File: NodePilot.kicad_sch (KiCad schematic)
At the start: 33 parts, among them K1 SRD-05VDC-SL-C, Q1 2N3904, Q2 2N3904, Q3 2N3904, Q4 2N3904, T1 1:1 600R, T2 1:1 600R, U1 PC817, U2 PC817

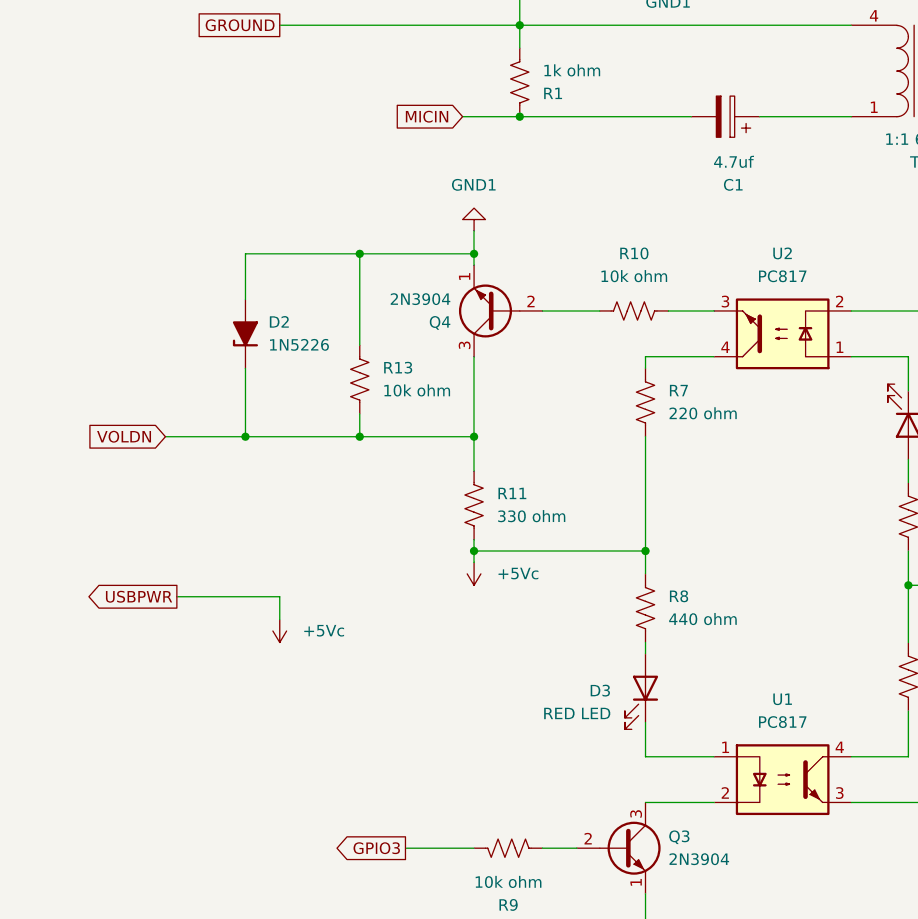
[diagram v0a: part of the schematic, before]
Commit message: usb instead of usbinvert
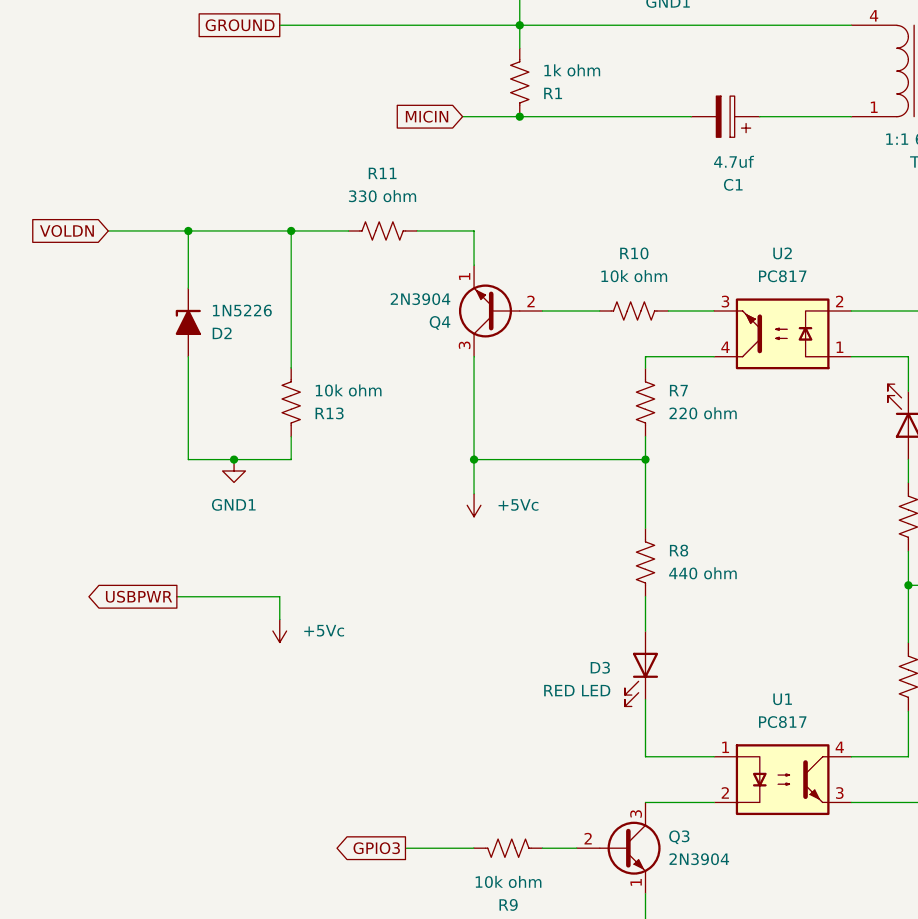
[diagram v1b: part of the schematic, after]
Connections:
- net +5Vc: now also Q4.3 (C); no longer R11.2
- net GND1: no longer Q4.1 (E)
- net VOLDN: no longer Q4.3 (C)
- new net: Q4.1 (E), R11.2
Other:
- moved on the sheet: D2, D3, R13, R8

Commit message: name fix
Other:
- title: NodePilot By Radiosanda -> NodePilot By S21TIP
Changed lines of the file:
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@@
 	(paper "A4")
 	(title_block
-		(title "NodePilot By Radiosanda")
+		(title "NodePilot By S21TIP")
 		(date "2025-11-30")
 		(rev "2.1")

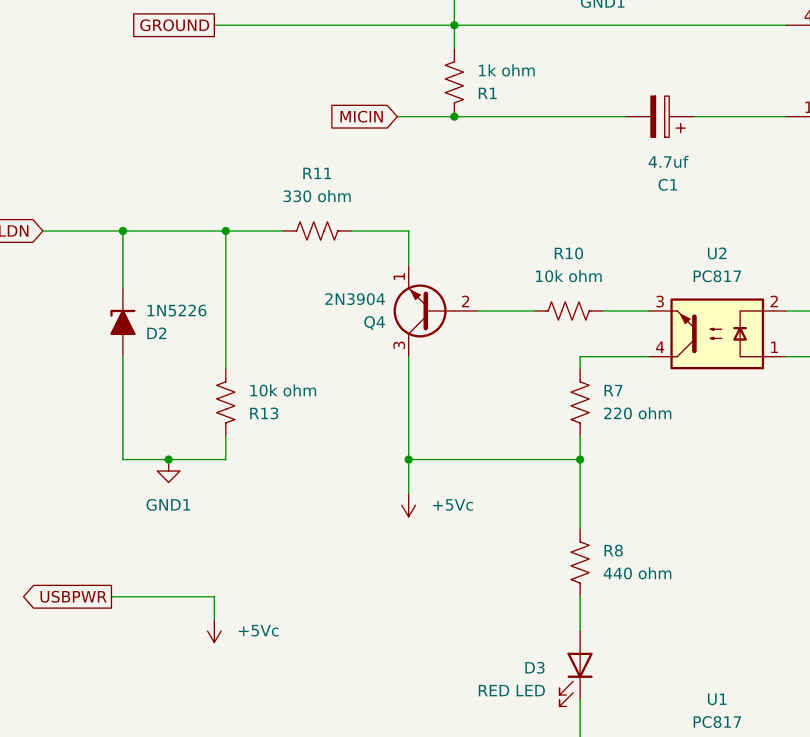
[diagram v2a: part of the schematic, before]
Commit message: 3904 load config fix
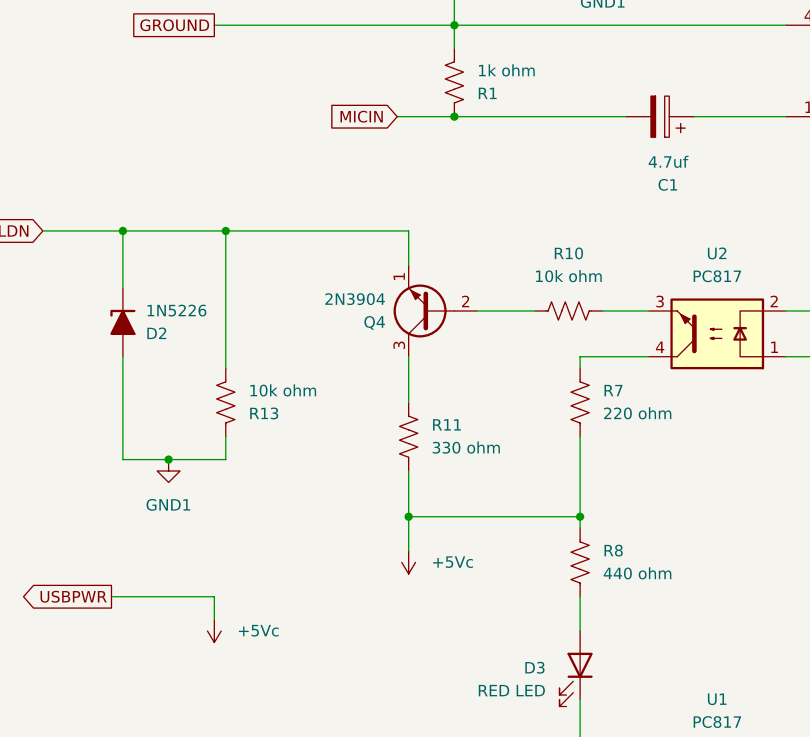
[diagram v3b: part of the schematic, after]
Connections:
- net +5Vc: now also R11.2; no longer Q4.3 (C)
- net VOLDN: now also Q4.1 (E); no longer R11.1
- new net: Q4.3 (C), R11.1
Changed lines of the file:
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@@
-	)
-	(junction
-		(at 72.39 105.41)
-		(diameter 0)
-		(color 0 0 0 0)
 	)
 	(junction
@@
 	)
 	(junction
+		(at 72.39 111.76)
+		(diameter 0)
+		(color 0 0 0 0)
+	)
+	(junction
 		(at 93.98 46.99)
 		(diameter 0)
@@
 	)
 	(junction
-		(at 91.44 105.41)
-		(diameter 0)
-		(color 0 0 0 0)
-	)
-	(junction
 		(at 134.62 119.38)
 		(diameter 0)
@@
 	)
 	(junction
+		(at 91.44 111.76)
+		(diameter 0)
+		(color 0 0 0 0)
+	)
+	(junction
 		(at 77.47 67.31)
 		(diameter 0)
@@
 	(wire
 		(pts
-			(xy 91.44 102.87) (xy 91.44 105.41)
-		)
-		(stroke
-			(width 0)
-			(type default)
-		)
-	)
-	(wire
-		(pts
 			(xy 156.21 93.98) (xy 151.13 93.98)
 		)
@@
 	(wire
 		(pts
+			(xy 91.44 111.76) (xy 91.44 113.03)
+		)
+		(stroke
+			(width 0)
+			(type default)
+		)
+	)
+	(wire
+		(pts
 			(xy 77.47 57.15) (xy 114.3 57.15)
 		)
@@
 	(wire
 		(pts
-			(xy 72.39 105.41) (xy 91.44 105.41)
+			(xy 72.39 111.76) (xy 91.44 111.76)
 		)
 		(stroke
@@
 	(wire
 		(pts
+			(xy 72.39 93.98) (xy 72.39 99.06)
+		)
+		(stroke
+			(width 0)
+			(type default)
+		)
+	)
+	(wire
+		(pts
 			(xy 72.39 80.01) (xy 72.39 83.82)
 		)
@@
 	(wire
 		(pts
+			(xy 72.39 111.76) (xy 72.39 115.57)
+		)
+		(stroke
+			(width 0)
+			(type default)
+		)
+	)
+	(wire
+		(pts
 			(xy 170.18 119.38) (xy 134.62 119.38)
 		)
@@
 	(wire
 		(pts
-			(xy 66.04 80.01) (xy 72.39 80.01)
-		)
-		(stroke
-			(width 0)
-			(type default)
-		)
-	)
-	(wire
-		(pts
 			(xy 71.12 67.31) (xy 77.47 67.31)
 		)
@@
 	(wire
 		(pts
-			(xy 72.39 93.98) (xy 72.39 105.41)
-		)
-		(stroke
-			(width 0)
-			(type default)
-		)
-	)
-	(wire
-		(pts
 			(xy 120.65 105.41) (xy 120.65 107.95)
 		)
@@
 	(wire
 		(pts
-			(xy 52.07 80.01) (xy 58.42 80.01)
+			(xy 52.07 80.01) (xy 72.39 80.01)
 		)
 		(stroke
@@
 	(wire
 		(pts
-			(xy 91.44 105.41) (xy 91.44 113.03)
-		)
-		(stroke
-			(width 0)
-			(type default)
-		)
-	)
-	(wire
-		(pts
 			(xy 170.18 135.89) (xy 170.18 138.43)
 		)
@@
 	(wire
 		(pts
+			(xy 91.44 102.87) (xy 91.44 111.76)
+		)
+		(stroke
+			(width 0)
+			(type default)
+		)
+	)
+	(wire
+		(pts
 			(xy 40.64 80.01) (xy 40.64 86.36)
 		)
@@
 	(wire
 		(pts
+			(xy 72.39 106.68) (xy 72.39 111.76)
+		)
+		(stroke
+			(width 0)
+			(type default)
+		)
+	)
+	(wire
+		(pts
 			(xy 180.34 135.89) (xy 180.34 139.7)
 		)
@@
 		(pts
 			(xy 144.78 67.31) (xy 157.48 67.31)
-		)
-		(stroke
-			(width 0)
-			(type default)
-		)
-	)
-	(wire
-		(pts
-			(xy 72.39 105.41) (xy 72.39 109.22)
 		)
 		(stroke
@@
 	(symbol
 		(lib_id "power:+5V")
-		(at 72.39 109.22 180)
+		(at 72.39 115.57 180)
 		(unit 1)
 		(exclude_from_sim no)
@@
 		(fields_autoplaced yes)
 		(property "Reference" "#PWR0101"
-			(at 72.39 105.41 0)
+			(at 72.39 111.76 0)
 			(effects
 				(font
@@
 		)
 		(property "Value" "+5Vc"
-			(at 74.93 110.4899 0)
+			(at 74.93 116.8399 0)
 			(effects
 				(font
@@
 		)
 		(property "Footprint" ""
-			(at 72.39 109.22 0)
+			(at 72.39 115.57 0)
 			(effects
 				(font
@@
 		)
 		(property "Datasheet" ""
-			(at 72.39 109.22 0)
+			(at 72.39 115.57 0)
 			(effects
 				(font
@@
 		)
 		(property "Description" "Power symbol creates a global label with name \"+5V\""
-			(at 72.39 109.22 0)
+			(at 72.39 115.57 0)
 			(effects
 				(font
@@
 	)
 	(symbol
-		(lib_id "Device:R_US")
-		(at 62.23 80.01 90)
-		(unit 1)
-		(exclude_from_sim no)
-		(in_bom yes)
-		(on_board yes)
-		(dnp no)
-		(fields_autoplaced yes)
-		(property "Reference" "R11"
-			(at 62.23 73.66 90)
-			(effects
-				(font
-					(size 1.27 1.27)
-				)
-			)
-		)
-		(property "Value" "330 ohm"
-			(at 62.23 76.2 90)
-			(effects
-				(font
-					(size 1.27 1.27)
-				)
-			)
-		)
-		(property "Footprint" ""
-			(at 62.484 78.994 90)
-			(effects
-				(font
-					(size 1.27 1.27)
-				)
-				(hide yes)
-			)
-		)
-		(property "Datasheet" "~"
-			(at 62.23 80.01 0)
-			(effects
-				(font
-					(size 1.27 1.27)
-				)
-				(hide yes)
-			)
-		)
-		(property "Description" "Resistor, US symbol"
-			(at 62.23 80.01 0)
-			(effects
-				(font
-					(size 1.27 1.27)
-				)
-				(hide yes)
-			)
-		)
-		(pin "1"
-		)
-		(pin "2"
-		)
-		(instances
-			(project ""
-				(path "/feb6dcc4-ba57-4640-ad64-1efd302ce012"
-					(reference "R11")
-					(unit 1)
-				)
-			)
-		)
-	)
-	(symbol
 		(lib_id "power:+5V")
 		(at 204.47 148.59 180)
@@
 					(unit 1)
 				)
+			)
+		)
+	)
+	(symbol
+		(lib_id "Device:R_US")
+		(at 72.39 102.87 0)
+		(unit 1)
+		(exclude_from_sim no)
+		(in_bom yes)
+		(on_board yes)
+		(dnp no)
+		(fields_autoplaced yes)
+		(property "Reference" "R11"
+			(at 74.93 101.5999 0)
+			(effects
+				(font
+					(size 1.27 1.27)
+				)
+				(justify left)
+			)
+		)
+		(property "Value" "330 ohm"
+			(at 74.93 104.1399 0)
+			(effects
+				(font
+					(size 1.27 1.27)
+				)
+				(justify left)
+			)
+		)
+		(property "Footprint" ""
+			(at 73.406 103.124 90)
+			(effects
+				(font
+					(size 1.27 1.27)
+				)
+				(hide yes)
+			)
+		)
+		(property "Datasheet" "~"
+			(at 72.39 102.87 0)
+			(effects
+				(font
+					(size 1.27 1.27)
+				)
+				(hide yes)
+			)
+		)
+		(property "Description" "Resistor, US symbol"
+			(at 72.39 102.87 0)
+			(effects
+				(font
+					(size 1.27 1.27)
+				)
+				(hide yes)
+			)
+		)
+		(pin "1"
+		)
+		(pin "2"
+		)
+		(instances
+			(project ""
+				(path "/feb6dcc4-ba57-4640-ad64-1efd302ce012"
+					(reference "R11")
+					(unit 1)
+				)

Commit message: version 3.0
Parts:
- removed Q2: 2N3904, Package_TO_SOT_THT:TO-92_Inline, symbol Transistor_BJT:2N3904
- removed R5: 10k ohm, symbol Device:R_US
- removed R6: 220 ohm, symbol Device:R_US
- removed R8: 440 ohm, symbol Device:R_US
- removed U1: PC817, Package_DIP:DIP-4_W7.62mm, symbol Isolator:PC817
- R2: value 440 ohm -> 330 ohm
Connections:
- net +5Vc: now also K1.5
- net +5Vr: no longer K1.5, R4.1
- net at R4.2: now also K1.2
- net at D3.1 (K): now also Q3.3 (C)
- net at D3.2 (A): now also R4.1
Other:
- moved on the sheet: K1, Q3, R9

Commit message: ver 3.1
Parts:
- removed R7: 220 ohm, symbol Device:R_US
- R13: value 10k ohm -> 22k ohm
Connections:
- net at U2.4: now also Q4.3 (C), R11.1
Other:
- moved on the sheet: R11
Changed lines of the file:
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@@
 	(title_block
 		(title "NodePilot By S21TIP")
-		(date "2025-12-11")
-		(rev "3.0")
+		(date "2025-12-12")
+		(rev "3.1")
+	)
+	(junction
+		(at 86.36 133.35)
+		(diameter 0)
+		(color 0 0 0 0)
 	)
 	(junction
@@
 	)
 	(junction
-		(at 81.28 111.76)
+		(at 81.28 93.98)
 		(diameter 0)
 		(color 0 0 0 0)
@@
 	)
 	(junction
-		(at 91.44 111.76)
-		(diameter 0)
-		(color 0 0 0 0)
-	)
-	(junction
 		(at 40.64 80.01)
 		(diameter 0)
@@
 	(wire
 		(pts
-			(xy 91.44 133.35) (xy 146.05 133.35)
-		)
-		(stroke
-			(width 0)
-			(type default)
-		)
-	)
-	(wire
-		(pts
 			(xy 137.16 67.31) (xy 129.54 67.31)
 		)
@@
 	(wire
 		(pts
-			(xy 81.28 111.76) (xy 91.44 111.76)
+			(xy 81.28 133.35) (xy 86.36 133.35)
 		)
 		(stroke
@@
 	(wire
 		(pts
-			(xy 99.06 93.98) (xy 91.44 93.98)
-		)
-		(stroke
-			(width 0)
-			(type default)
-		)
-	)
-	(wire
-		(pts
 			(xy 77.47 59.69) (xy 77.47 57.15)
 		)
@@
 	(wire
 		(pts
-			(xy 72.39 111.76) (xy 81.28 111.76)
-		)
-		(stroke
-			(width 0)
-			(type default)
-		)
-	)
-	(wire
-		(pts
 			(xy 80.01 88.9) (xy 86.36 88.9)
 		)
@@
 	(wire
 		(pts
-			(xy 72.39 93.98) (xy 72.39 99.06)
+			(xy 72.39 80.01) (xy 72.39 83.82)
 		)
 		(stroke
@@
 	(wire
 		(pts
-			(xy 72.39 80.01) (xy 72.39 83.82)
+			(xy 81.28 93.98) (xy 81.28 99.06)
 		)
 		(stroke
@@
 	(wire
 		(pts
-			(xy 81.28 111.76) (xy 81.28 115.57)
+			(xy 86.36 133.35) (xy 86.36 135.89)
 		)
 		(stroke
@@
 	(wire
 		(pts
-			(xy 91.44 93.98) (xy 91.44 95.25)
-		)
-		(stroke
-			(width 0)
-			(type default)
-		)
-	)
-	(wire
-		(pts
 			(xy 93.98 88.9) (xy 99.06 88.9)
 		)
@@
 	(wire
 		(pts
+			(xy 86.36 133.35) (xy 146.05 133.35)
+		)
+		(stroke
+			(width 0)
+			(type default)
+		)
+	)
+	(wire
+		(pts
 			(xy 157.48 67.31) (xy 157.48 69.85)
 		)
@@
 	(wire
 		(pts
+			(xy 81.28 93.98) (xy 99.06 93.98)
+		)
+		(stroke
+			(width 0)
+			(type default)
+		)
+	)
+	(wire
+		(pts
 			(xy 140.97 49.53) (xy 140.97 46.99)
 		)
@@
 	(wire
 		(pts
-			(xy 91.44 102.87) (xy 91.44 111.76)
+			(xy 40.64 80.01) (xy 40.64 86.36)
 		)
 		(stroke
@@
 	(wire
 		(pts
-			(xy 40.64 80.01) (xy 40.64 86.36)
+			(xy 77.47 46.99) (xy 77.47 57.15)
 		)
 		(stroke
@@
 	(wire
 		(pts
-			(xy 77.47 46.99) (xy 77.47 57.15)
+			(xy 218.44 57.15) (xy 218.44 101.6)
 		)
 		(stroke
@@
 	(wire
 		(pts
-			(xy 218.44 57.15) (xy 218.44 101.6)
+			(xy 40.64 80.01) (xy 52.07 80.01)
 		)
 		(stroke
@@
 	(wire
 		(pts
-			(xy 40.64 80.01) (xy 52.07 80.01)
+			(xy 189.23 73.66) (xy 199.39 73.66)
 		)
 		(stroke
@@
 	(wire
 		(pts
-			(xy 189.23 73.66) (xy 199.39 73.66)
+			(xy 81.28 93.98) (xy 72.39 93.98)
 		)
 		(stroke
@@
 	(wire
 		(pts
-			(xy 72.39 106.68) (xy 72.39 111.76)
+			(xy 81.28 106.68) (xy 81.28 133.35)
 		)
 		(stroke
@@
 	(wire
 		(pts
-			(xy 91.44 111.76) (xy 91.44 133.35)
-		)
-		(stroke
-			(width 0)
-			(type default)
-		)
-	)
-	(wire
-		(pts
 			(xy 93.98 46.99) (xy 114.3 46.99)
 		)
@@
 	(symbol
 		(lib_id "power:+5V")
-		(at 81.28 115.57 180)
+		(at 86.36 135.89 180)
 		(unit 1)
 		(exclude_from_sim no)
@@
 		(fields_autoplaced yes)
 		(property "Reference" "#PWR0101"
-			(at 81.28 111.76 0)
+			(at 86.36 132.08 0)
 			(effects
 				(font
@@
 		)
 		(property "Value" "+5Vc"
-			(at 83.82 116.8399 0)
+			(at 88.9 137.1599 0)
 			(effects
 				(font
@@
 		)
 		(property "Footprint" ""
-			(at 81.28 115.57 0)
+			(at 86.36 135.89 0)
 			(effects
 				(font
@@
 		)
 		(property "Datasheet" ""
-			(at 81.28 115.57 0)
+			(at 86.36 135.89 0)
 			(effects
 				(font
@@
 		)
 		(property "Description" "Power symbol creates a global label with name \"+5V\""
-			(at 81.28 115.57 0)
+			(at 86.36 135.89 0)
 			(effects
 				(font
@@
 	(symbol
 		(lib_id "Device:R_US")
-		(at 72.39 102.87 0)
+		(at 81.28 102.87 0)
 		(unit 1)
 		(exclude_from_sim no)
@@
 		(fields_autoplaced yes)
 		(property "Reference" "R11"
-			(at 74.93 101.5999 0)
+			(at 83.82 101.5999 0)
 			(effects
 				(font
@@
 		)
 		(property "Value" "330 ohm"
-			(at 74.93 104.1399 0)
+			(at 83.82 104.1399 0)
 			(effects
 				(font
@@
 		)
 		(property "Footprint" ""
-			(at 73.406 103.124 90)
+			(at 82.296 103.124 90)
 			(effects
 				(font
@@
 		)
 		(property "Datasheet" "~"
-			(at 72.39 102.87 0)
+			(at 81.28 102.87 0)
 			(effects
 				(font
@@
 		)
 		(property "Description" "Resistor, US symbol"
-			(at 72.39 102.87 0)
+			(at 81.28 102.87 0)
 			(effects
 				(font
@@
 	)
 	(symbol
-		(lib_id "Device:R_US")
-		(at 91.44 99.06 0)
-		(unit 1)
-		(exclude_from_sim no)
-		(in_bom yes)
-		(on_board yes)
-		(dnp no)
-		(fields_autoplaced yes)
-		(property "Reference" "R7"
-			(at 93.98 97.7899 0)
-			(effects
-				(font
-					(size 1.27 1.27)
-				)
-				(justify left)
-			)
-		)
-		(property "Value" "220 ohm"
-			(at 93.98 100.3299 0)
-			(effects
-				(font
-					(size 1.27 1.27)
-				)
-				(justify left)
-			)
-		)
-		(property "Footprint" ""
-			(at 92.456 99.314 90)
-			(effects
-				(font
-					(size 1.27 1.27)
-				)
-				(hide yes)
-			)
-		)
-		(property "Datasheet" "~"
-			(at 91.44 99.06 0)
-			(effects
-				(font
-					(size 1.27 1.27)
-				)
-				(hide yes)
-			)
-		)
-		(property "Description" "Resistor, US symbol"
-			(at 91.44 99.06 0)
-			(effects
-				(font
-					(size 1.27 1.27)
-				)
-				(hide yes)
-			)
-		)
-		(pin "1"
-		)
-		(pin "2"
-		)
-		(instances
-			(project "NodePilot"
-				(path "/feb6dcc4-ba57-4640-ad64-1efd302ce012"
-					(reference "R7")
-					(unit 1)
-				)
-			)
-		)
-	)
-	(symbol
 		(lib_id "Relay:SANYOU_SRD_Form_C")
 		(at 151.13 140.97 0)
@@
 			)
 		)
-		(property "Value" "10k ohm"
+		(property "Value" "22k ohm"
 			(at 54.61 97.7901 0)
 			(effects
